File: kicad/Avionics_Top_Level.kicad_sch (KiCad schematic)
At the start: 10 parts, among them U1 MAX31856, U10 Type_K, U2 MAX31856, U3 MAX31856, U4 MAX31856, U5 MAX31856, U6 Type_K, U7 Type_K, U8 Type_K, U9 Type_K

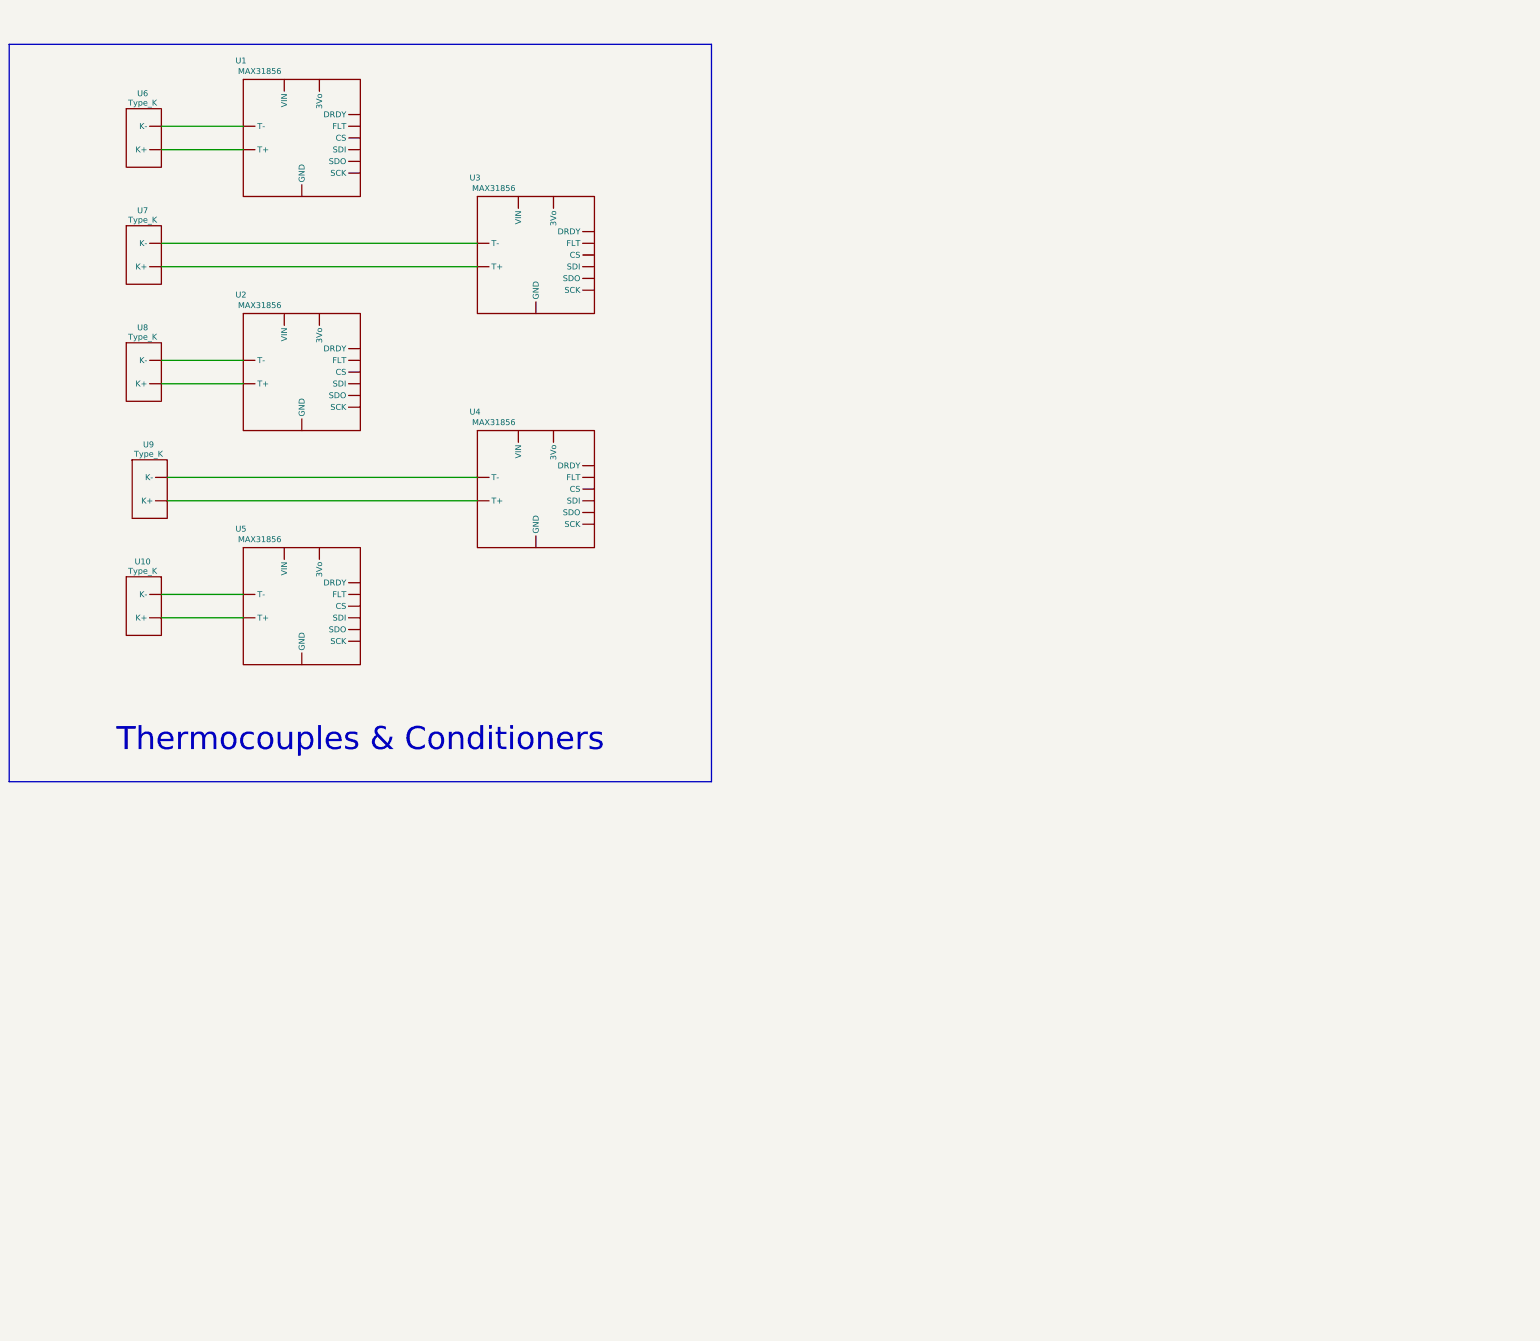
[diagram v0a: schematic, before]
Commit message: continue temp and start pressure sensors
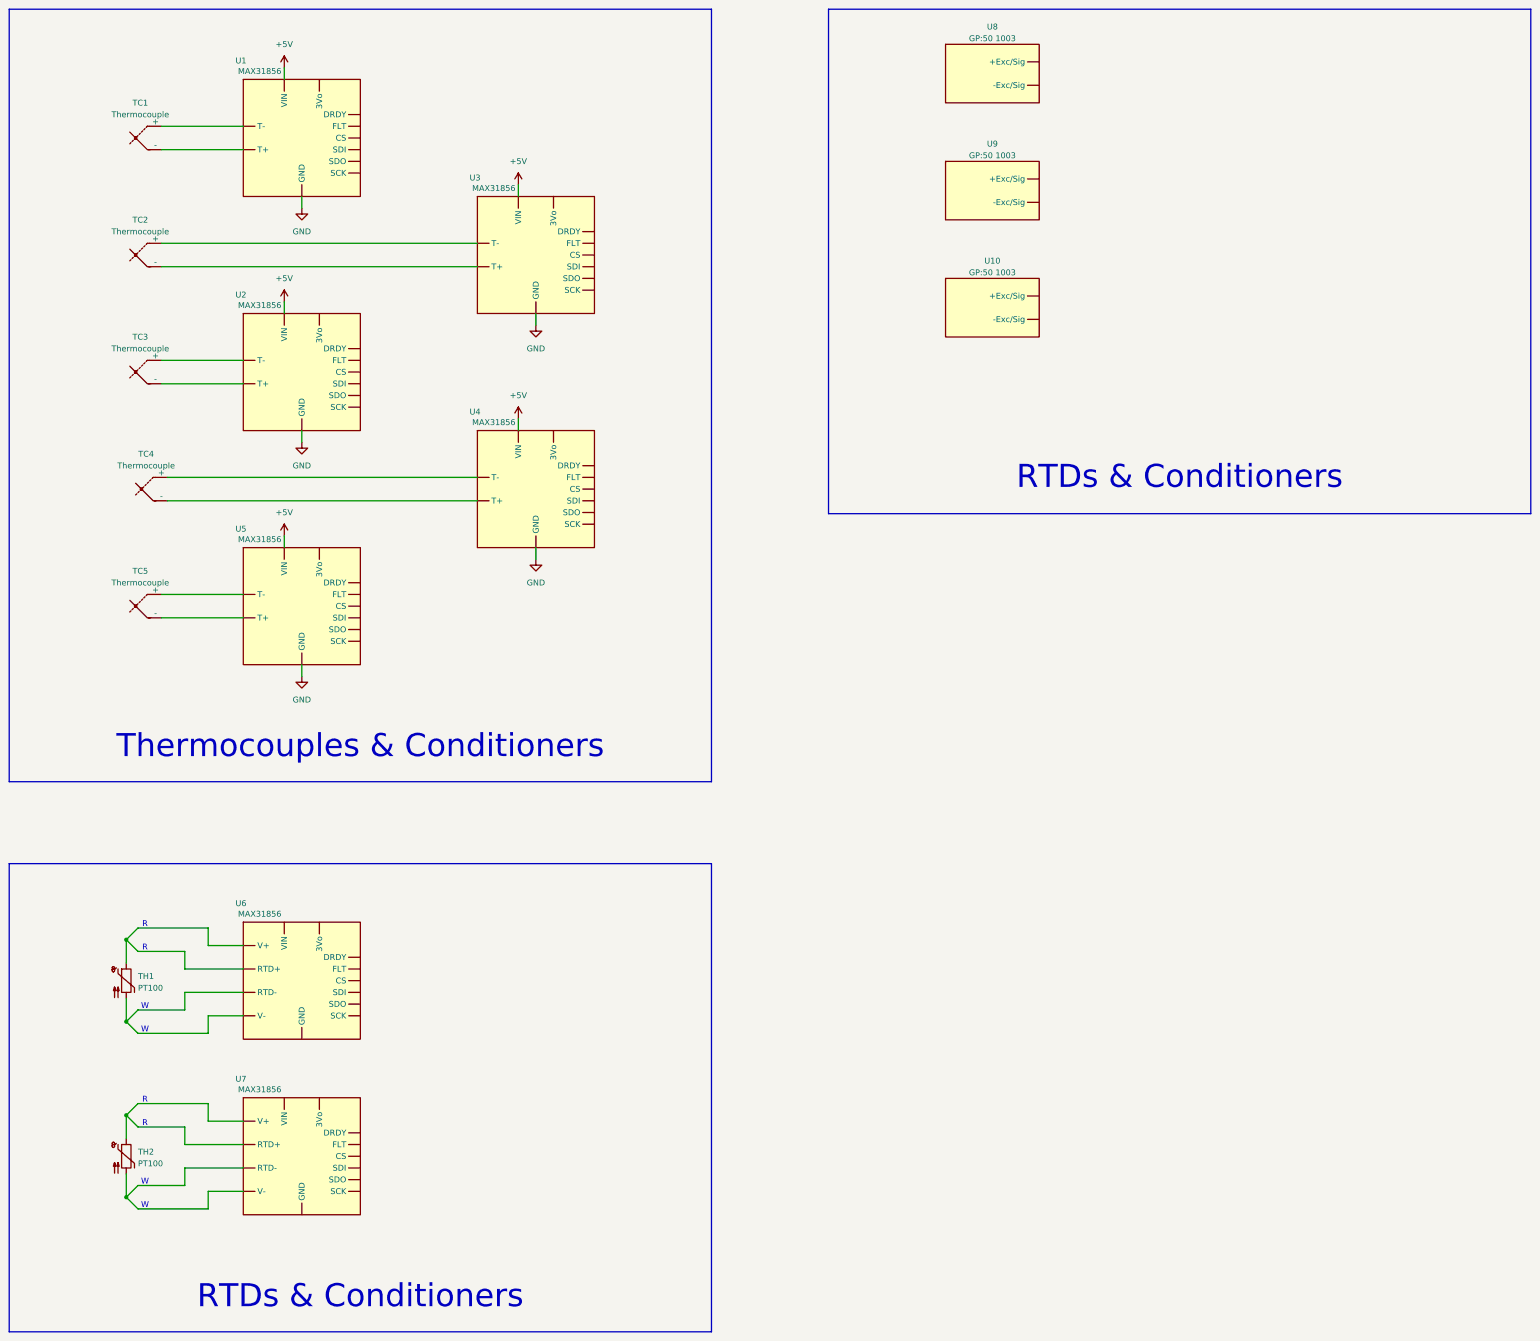
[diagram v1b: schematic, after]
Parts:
- removed U10, U6, U7, U8, U9: Type_K, symbol JRPD_Avionics:Type_K_Thermocouple
- added TC1, TC2, TC3, TC4, TC5: Thermocouple, Package_SO:MSOP-8_3x3mm_P0.65mm, symbol Device:Thermocouple
- added TH1, TH2: PT100, Package_SO:SSOP-20_5.3x7.2mm_P0.65mm, symbol Sensor_Temperature:PT100
- added U10, U8, U9: GP:50 1003, symbol JRPD_Avionics:GP{colon}50_Pressure_Sensor
- added U6, U7: MAX31856, symbol JRPD_Avionics:RTD_Conditioner
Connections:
- net GND: now reaches U1. (SCK)
- net GND: now also U2. (SCK), U3. (SCK), U4. (SCK), U5. (SCK)
- new net: TC3.1 (+), U2. (SCK)
- new net: TC3.2 (-), U2. (SCK)
- new net: TC5.1 (+), U5. (SCK)
- new net: TC5.2 (-), U5. (SCK)
- new net: TH2.1, U7. (SCK)
- new net: TH2.2, U7. (SCK)
- new net: TH1.1, U6. (SCK)
- new net: TH1.2, U6. (SCK)
- new net: TC1.1 (+), U1. (SCK)
- new net: TC1.2 (-), U1. (SCK)
- new net: TC2.1 (+), U3. (SCK)
- new net: TC2.2 (-), U3. (SCK)
- new net: TC4.1 (+), U4. (SCK)
- new net: TC4.2 (-), U4. (SCK)
- new net +5V: U1. (SCK), U2. (SCK), U3. (SCK), U4. (SCK), U5. (SCK)
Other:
- note added: "R"
- note added: "RTDs & Conditioners"
- note added: "W"
